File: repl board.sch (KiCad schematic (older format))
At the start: 24 parts, among them IC1 SN74HC42D, IC2 SN74HC42D, J2 Conn_01x16, J3 Conn_01x16, SW2 SW_Reed, U1 ATmega32U2-AU, Y1 ABM8G-16.000MHZ-4Y-T3

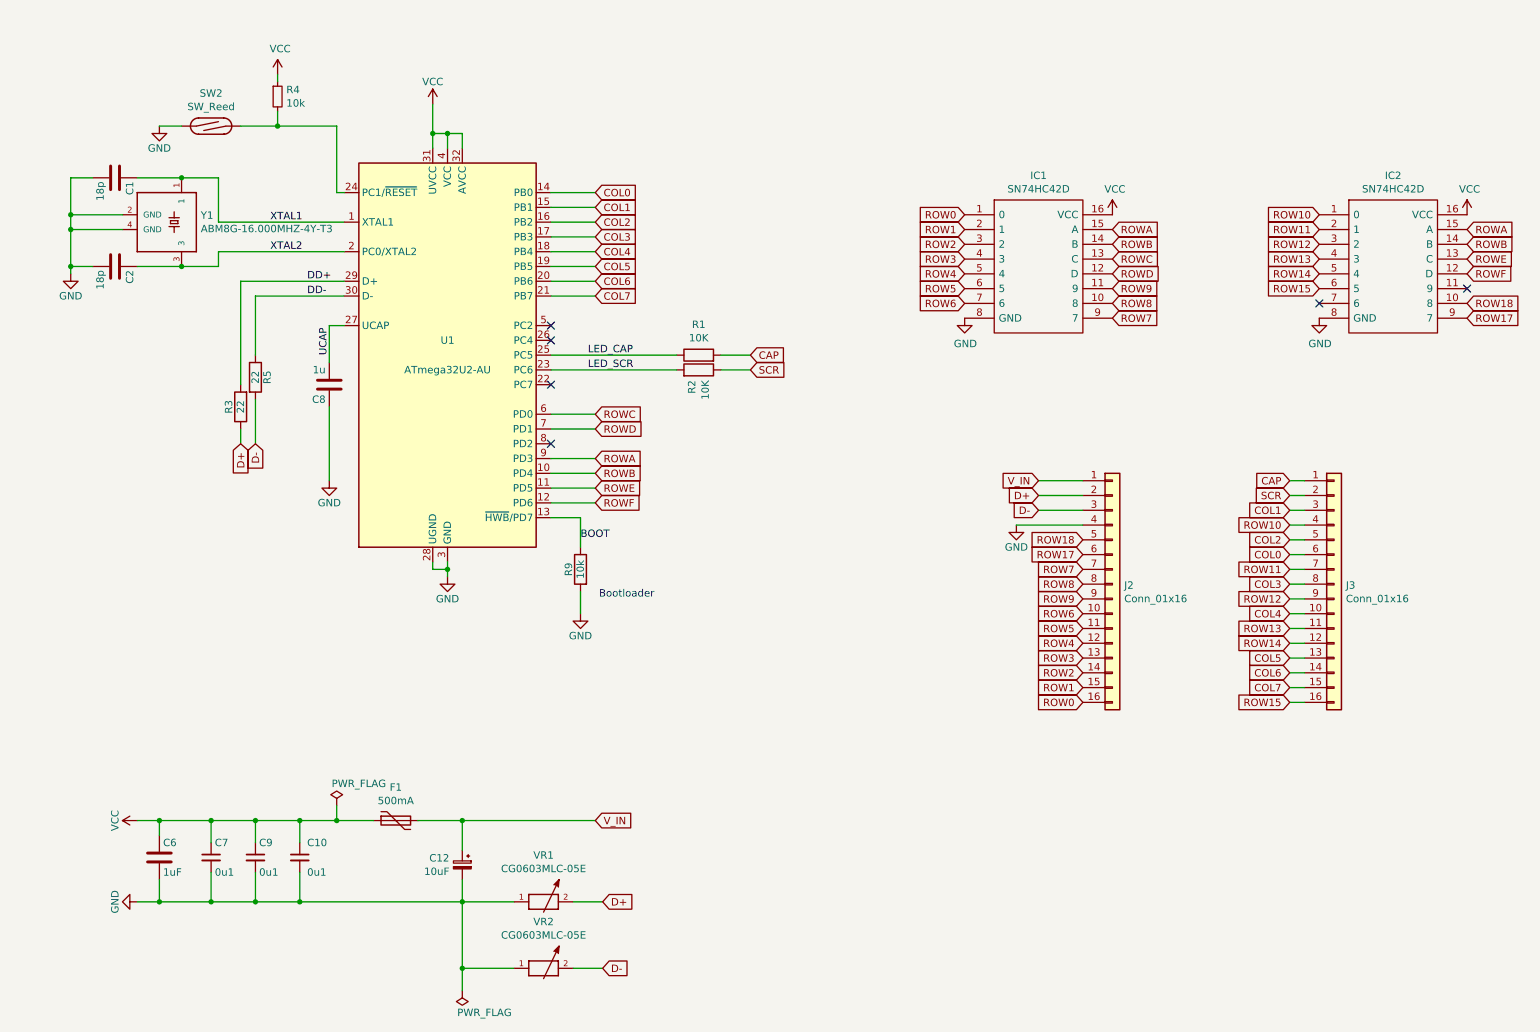
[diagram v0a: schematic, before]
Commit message: Fix chrystal
Fix Chrystal footprint, added ICSP header
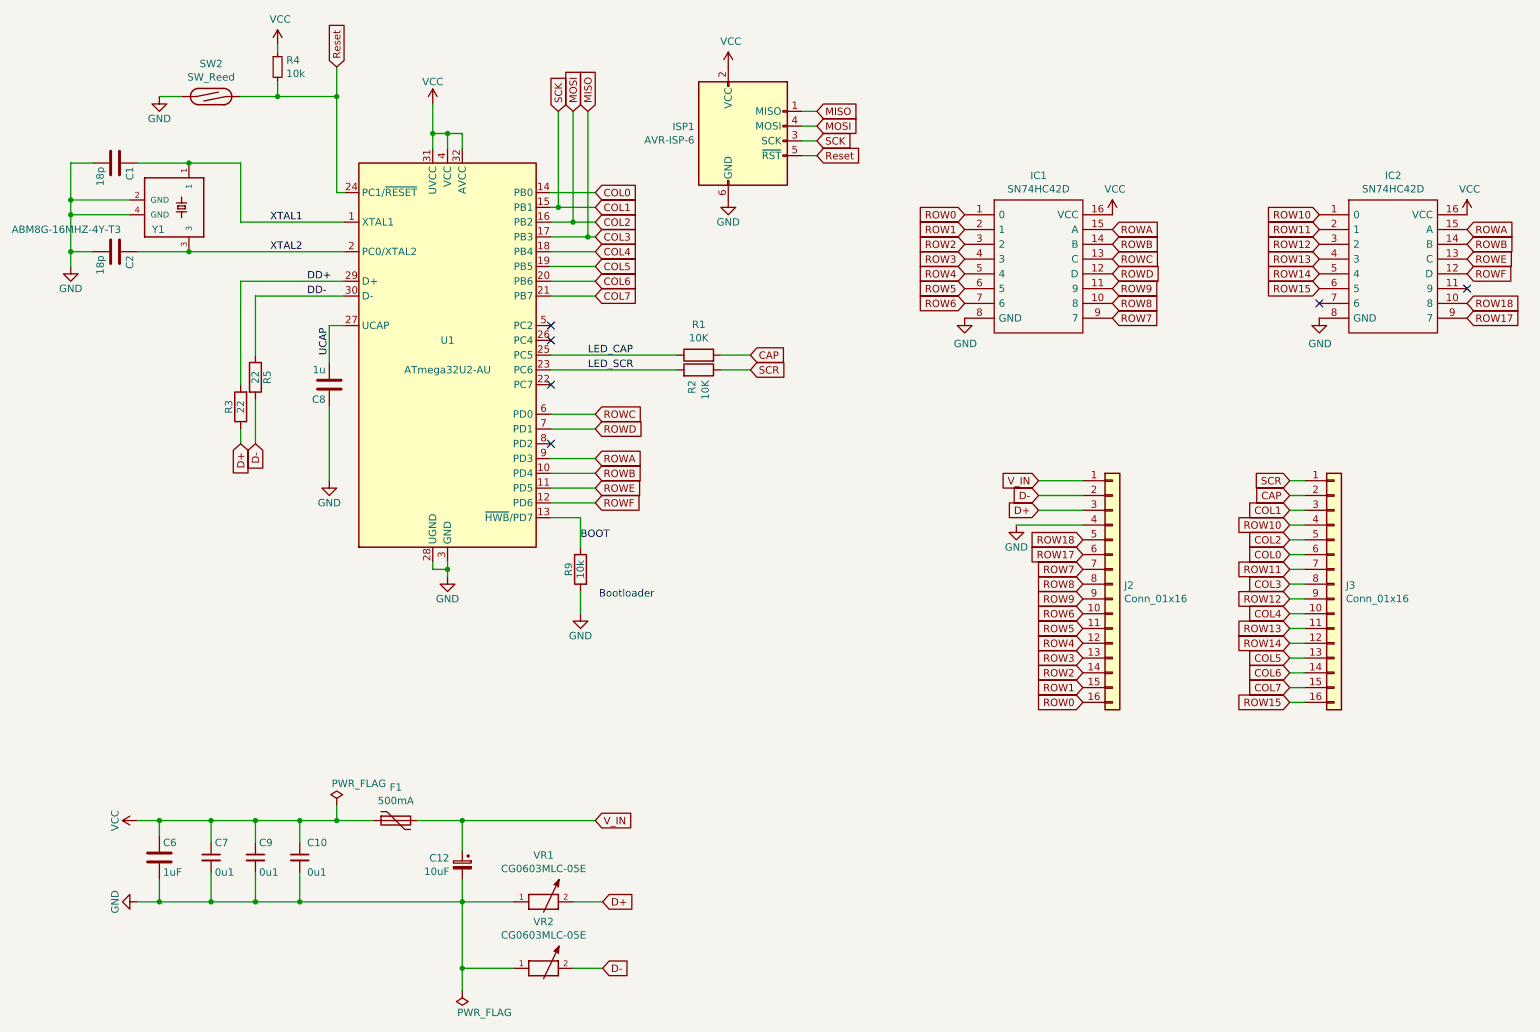
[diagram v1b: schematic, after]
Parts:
- added ISP1: AVR-ISP-6, Connector_PinHeader_2.54mm:PinHeader_1x06_P2.54mm_Vertical, symbol Connector:AVR-ISP-6
- Y1: value ABM8G-16.000MHZ-4Y-T3 -> ABM8G-16MHZ-4Y-T3; footprint Keyboard Library:OSCSC320X250X100N -> OSCSC320X250X100N
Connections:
- net CAP: now also J3.2 (Pin_2); no longer J3.1 (Pin_1)
- net COL1: now also ISP1.3 (SCK)
- net COL2: now also ISP1.4 (MOSI)
- net COL3: now also ISP1.1 (MISO)
- net D+: now also J2.3 (Pin_3); no longer J2.2 (Pin_2)
- net D-: now also J2.2 (Pin_2); no longer J2.3 (Pin_3)
- net GND: now also ISP1.6 (GND)
- net SCR: now also J3.1 (Pin_1); no longer J3.2 (Pin_2)
- net VCC: now also ISP1.2 (VCC)
- net Reset: now reaches R4.2, SW2.2, U1.24 (PC1/~RESET)
- net Reset: now also ISP1.5 (~RST)
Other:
- moved on the sheet: C1, C2, R4, SW2
